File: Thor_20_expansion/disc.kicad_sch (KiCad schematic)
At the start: 21 parts, among them J6 Conn_02x17_Counter_Clockwise, J7 Conn_02x17_Counter_Clockwise, U10 74LS04, U11 74LS05, U12 74LS638, U13 GAL16V8, U15 74LS245, U38 FDC_WD1772, U40 74LS05, U41 74LS03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

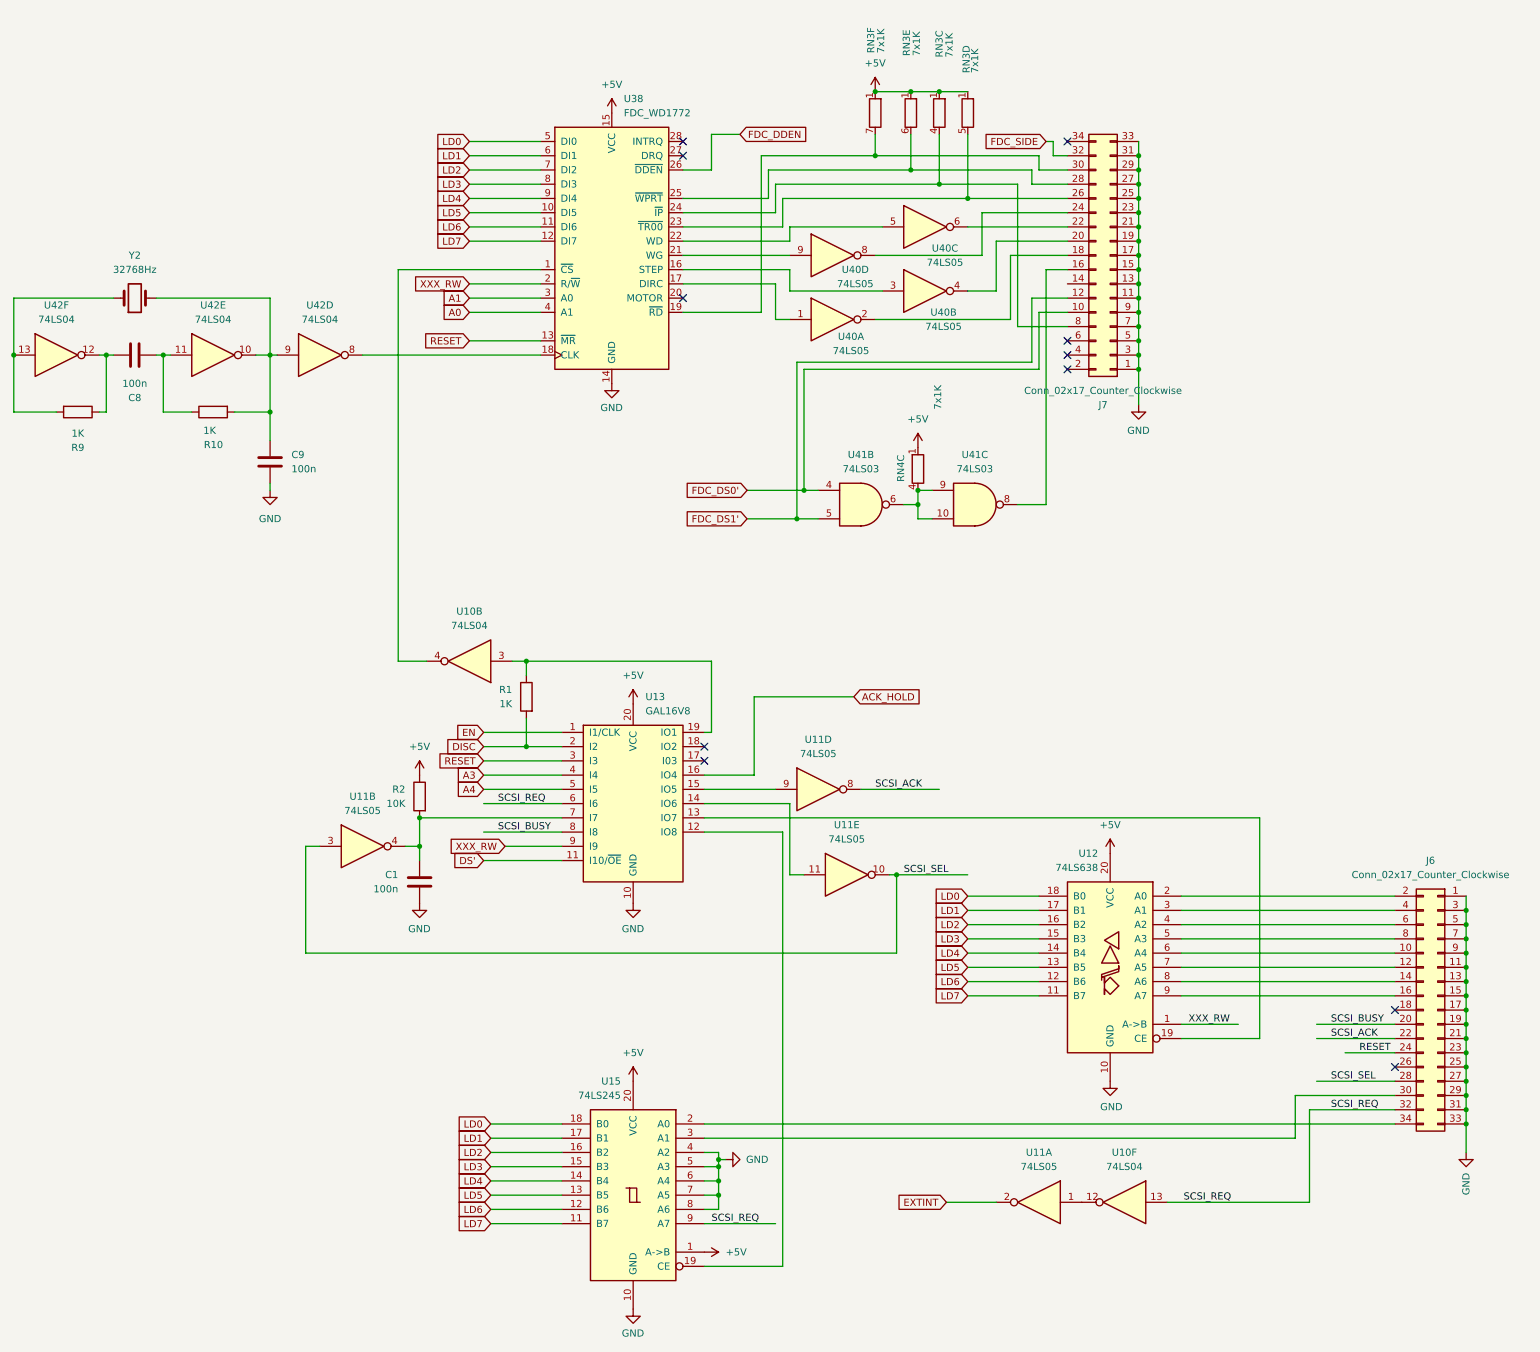
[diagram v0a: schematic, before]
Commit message: update schematic
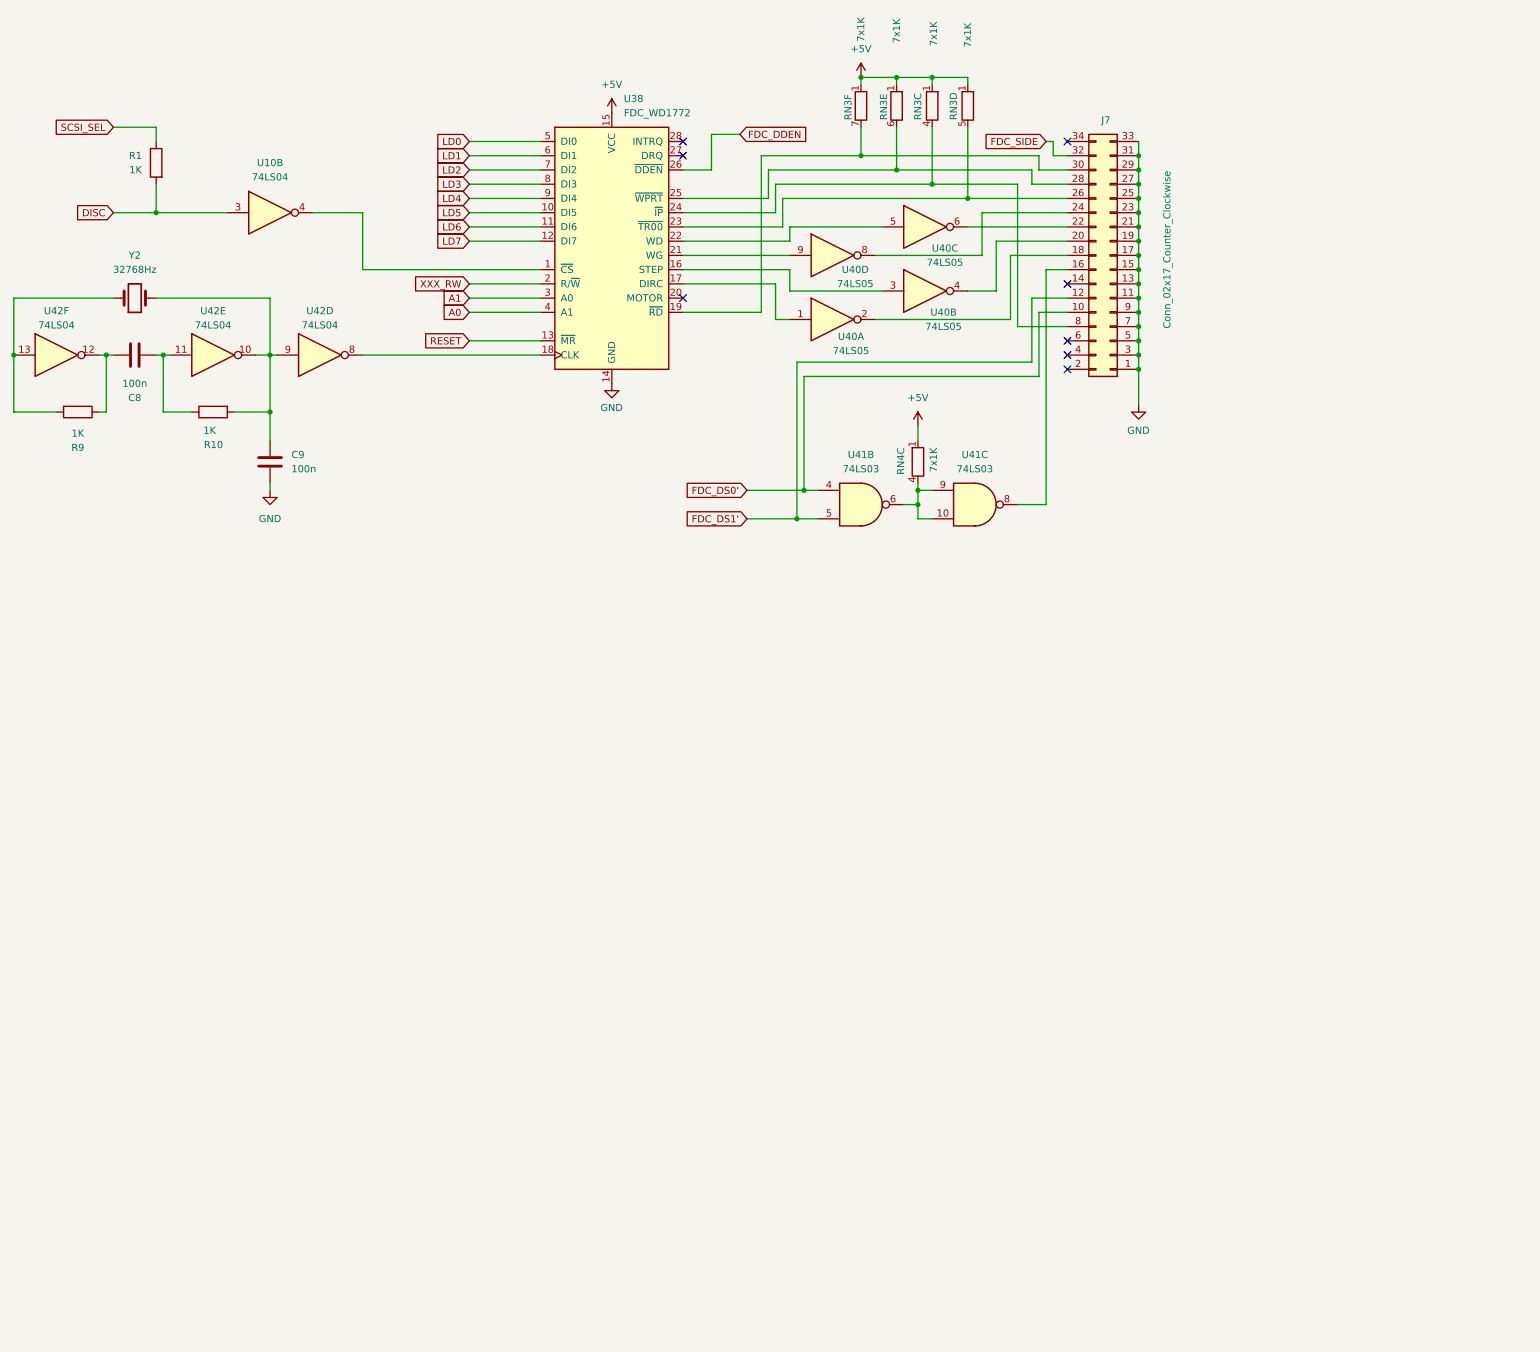
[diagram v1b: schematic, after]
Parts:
- removed C1: 100n, Capacitor_THT:C_Disc_D4.3mm_W1.9mm_P5.00mm, symbol Device:C
- removed J6: Conn_02x17_Counter_Clockwise, Connector_PinHeader_2.54mm:PinHeader_2x17_P2.54mm_Vertical, symbol Connector_Generic:Conn_02x17_Odd_Even
- removed R2: 10K, Resistor_THT:R_Axial_DIN0207_L6.3mm_D2.5mm_P10.16mm_Horizontal, symbol Device:R
- removed unit 6 of U10
- removed U11: 74LS05, Package_DIP:DIP-14_W7.62mm, symbol 74xx:74LS05
- removed U12: 74LS638, Package_DIP:DIP-20_W7.62mm, symbol 8bits:74LS638
- removed U13: GAL16V8, Package_DIP:DIP-20_W7.62mm, symbol Logic_Programmable:GAL16V8
- removed U15: 74LS245, Package_DIP:DIP-20_W7.62mm, symbol 74xx:74LS245
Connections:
- net DISC: now also U10.3
- net SCSI_SEL: now also R1.1
- no-connect marks 11 -> 8
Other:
- moved on the sheet: R1, RN3C, RN3D, RN3E, RN3F, RN4C, U10B
